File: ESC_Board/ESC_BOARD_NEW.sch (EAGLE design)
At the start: 165 parts, among them J3 AVR_SPI_PROG_3X2NS, U1 FQB27P06, U2 ATMEGA328P_TQFP, U3 FQB27P06, U4 PCA9685

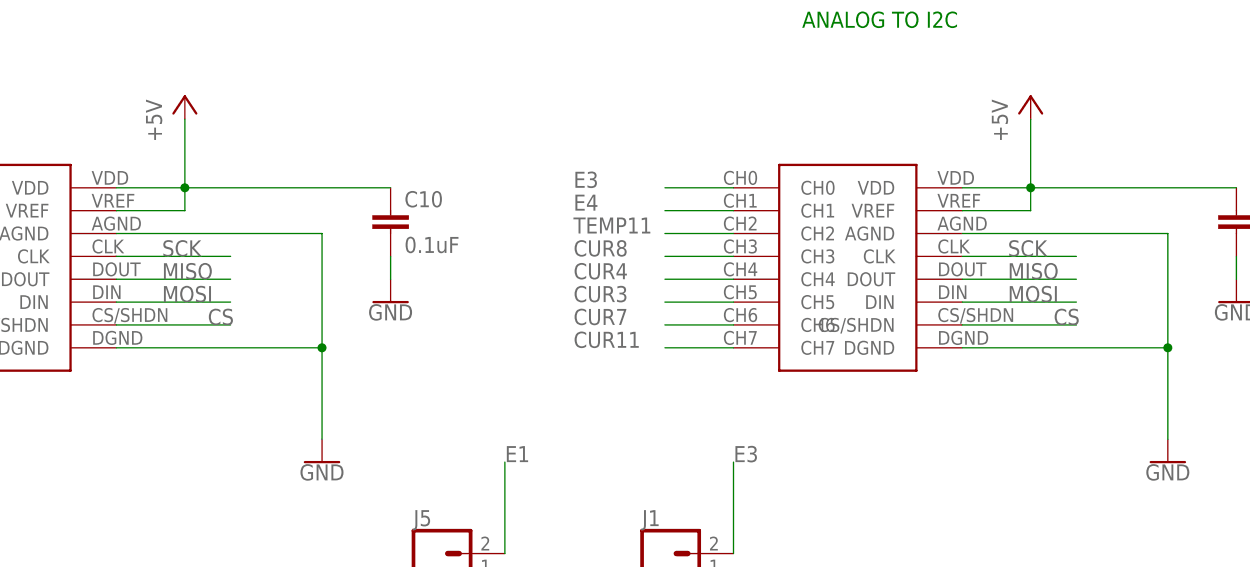
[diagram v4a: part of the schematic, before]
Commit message: Fixing gnd plane and fixing traces
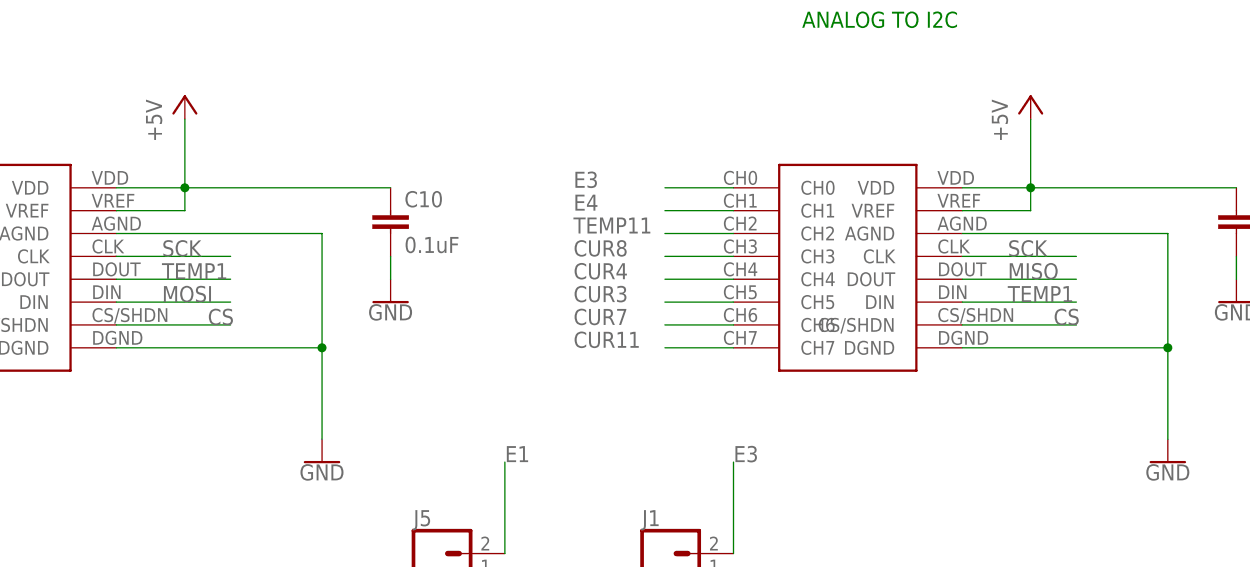
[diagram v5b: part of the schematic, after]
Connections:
- new net TEMP1: U$13.DIN, U$4.DOUT
- net MISO: no longer U$4.DOUT
- net MOSI: no longer U$13.DIN
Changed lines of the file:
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@@
 <?xml version="1.0" encoding="utf-8"?>
 <!DOCTYPE eagle SYSTEM "eagle.dtd">
-<eagle version="8.3.2">
+<eagle version="8.4.3">
 <drawing>
 <settings>
@@
 <label x="-40.64" y="304.8" size="1.778" layer="95"/>
 </segment>
-<segment>
-<pinref part="U$13" gate="G$1" pin="DIN"/>
-<wire x1="48.26" y1="304.8" x2="60.96" y2="304.8" width="0.1524" layer="91"/>
-<label x="53.34" y="304.8" size="1.778" layer="95"/>
-</segment>
 </net>
 <net name="MISO" class="0">
@@
 </segment>
 <segment>
-<pinref part="U$4" gate="G$1" pin="DOUT"/>
-<wire x1="-45.72" y1="307.34" x2="-33.02" y2="307.34" width="0.1524" layer="91"/>
-<label x="-40.64" y="307.34" size="1.778" layer="95"/>
-</segment>
-<segment>
 <pinref part="U$13" gate="G$1" pin="DOUT"/>
 <wire x1="48.26" y1="307.34" x2="60.96" y2="307.34" width="0.1524" layer="91"/>
@@
 </segment>
 </net>
+<net name="TEMP1" class="0">
+<segment>
+<pinref part="U$4" gate="G$1" pin="DOUT"/>
+<wire x1="-45.72" y1="307.34" x2="-33.02" y2="307.34" width="0.1524" layer="91"/>
+<label x="-40.64" y="307.34" size="1.778" layer="95"/>
+</segment>
+<segment>
+<pinref part="U$13" gate="G$1" pin="DIN"/>
+<wire x1="48.26" y1="304.8" x2="60.96" y2="304.8" width="0.1524" layer="91"/>
+<label x="53.34" y="304.8" size="1.778" layer="95"/>
+</segment>
+</net>

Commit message: Adding more test probes and cleaning up crooked traces
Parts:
- added J2, J7: (no value), SparkFun-Connectors:BANANA_CONN
- R10, R26, R27: value (none) -> 10k
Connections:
- net +12V: now also J2.1
- net GND: now also J7.1
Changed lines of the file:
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@@
 <part name="RESET" library="DiscreteComponents" deviceset="SWITCH" device="" value=""/>
 <part name="C11" library="rcl" library_urn="urn:adsk.eagle:library:334" deviceset="C-EU" device="C0603" package3d_urn="urn:adsk.eagle:package:23616/2" value="0.1uF"/>
-<part name="R10" library="SparkFun-Resistors" library_urn="urn:adsk.eagle:library:532" deviceset="RESISTOR" device="0603" package3d_urn="urn:adsk.eagle:package:39650/1" value=" "/>
+<part name="R10" library="SparkFun-Resistors" library_urn="urn:adsk.eagle:library:532" deviceset="RESISTOR" device="0603" package3d_urn="urn:adsk.eagle:package:39650/1" value="10k"/>
 <part name="GND27" library="supply1" deviceset="GND" device=""/>
 <part name="P+13" library="supply1" library_urn="urn:adsk.eagle:library:371" deviceset="+5V" device=""/>
@@
 <part name="C52" library="SparkFun-Capacitors" deviceset="0.1UF" device="-0603-25V-(+80/-20%)" value="0.1uF"/>
 <part name="GND69" library="SparkFun-PowerSymbols" deviceset="GND" device=""/>
-<part name="R26" library="rcl" library_urn="urn:adsk.eagle:library:334" deviceset="R-US_" device="R0603" package3d_urn="urn:adsk.eagle:package:23555/2"/>
-<part name="R27" library="rcl" library_urn="urn:adsk.eagle:library:334" deviceset="R-US_" device="R0603" package3d_urn="urn:adsk.eagle:package:23555/2"/>
+<part name="R26" library="rcl" library_urn="urn:adsk.eagle:library:334" deviceset="R-US_" device="R0603" package3d_urn="urn:adsk.eagle:package:23555/2" value="10k"/>
+<part name="R27" library="rcl" library_urn="urn:adsk.eagle:library:334" deviceset="R-US_" device="R0603" package3d_urn="urn:adsk.eagle:package:23555/2" value="10k"/>
 <part name="P+25" library="supply1" library_urn="urn:adsk.eagle:library:371" deviceset="+5V" device=""/>
 <part name="GND74" library="SparkFun-PowerSymbols" deviceset="GND" device=""/>
@@
 <part name="P14" library="SparkFun-Connectors" deviceset="M01" device="PTH"/>
 <part name="P15" library="SparkFun-Connectors" deviceset="M01" device="PTH"/>
+<part name="P+6" library="supply1" library_urn="urn:adsk.eagle:library:371" deviceset="+5V" device=""/>
+<part name="J2" library="SparkFun-Connectors" deviceset="BANANA_CONN" device=""/>
+<part name="J7" library="SparkFun-Connectors" deviceset="BANANA_CONN" device=""/>
+<part name="P+7" library="supply1" library_urn="urn:adsk.eagle:library:371" deviceset="+12V" device=""/>
+<part name="GND18" library="supply1" deviceset="GND" device=""/>
 </parts>
 <sheets>
@@
 <instance part="P14" gate="G$1" x="86.36" y="375.92" rot="MR0"/>
 <instance part="P15" gate="G$1" x="73.66" y="373.38" rot="MR0"/>
+<instance part="P+6" gate="1" x="-73.66" y="162.56"/>
+<instance part="J2" gate="G$1" x="340.36" y="406.4"/>
+<instance part="J7" gate="G$1" x="340.36" y="401.32"/>
+<instance part="P+7" gate="1" x="325.12" y="411.48"/>
+<instance part="GND18" gate="1" x="325.12" y="396.24"/>
 </instances>
 <busses>
@@
 <wire x1="5.08" y1="50.8" x2="5.08" y2="53.34" width="0.1524" layer="91"/>
 </segment>
+<segment>
+<pinref part="J7" gate="G$1" pin="1"/>
+<wire x1="337.82" y1="401.32" x2="325.12" y2="401.32" width="0.1524" layer="91"/>
+<label x="327.66" y="401.32" size="1.778" layer="95"/>
+<pinref part="GND18" gate="1" pin="GND"/>
+<wire x1="325.12" y1="401.32" x2="325.12" y2="398.78" width="0.1524" layer="91"/>
+</segment>
 </net>
 <net name="+12V" class="0">
@@
 <wire x1="5.08" y1="83.82" x2="5.08" y2="91.44" width="0.1524" layer="91"/>
 <pinref part="P+22" gate="1" pin="+12V"/>
+</segment>
+<segment>
+<pinref part="J2" gate="G$1" pin="1"/>
+<wire x1="337.82" y1="406.4" x2="325.12" y2="406.4" width="0.1524" layer="91"/>
+<label x="327.66" y="406.4" size="1.778" layer="95"/>
+<pinref part="P+7" gate="1" pin="+12V"/>
+<wire x1="325.12" y1="406.4" x2="325.12" y2="408.94" width="0.1524" layer="91"/>
 </segment>
 </net>
@@
 <wire x1="-73.66" y1="157.48" x2="-81.28" y2="157.48" width="0.1524" layer="91"/>
 <junction x="-73.66" y="157.48"/>
-</segment>
-<segment>
+<pinref part="P+6" gate="1" pin="+5V"/>
+</segment>
+<segment>

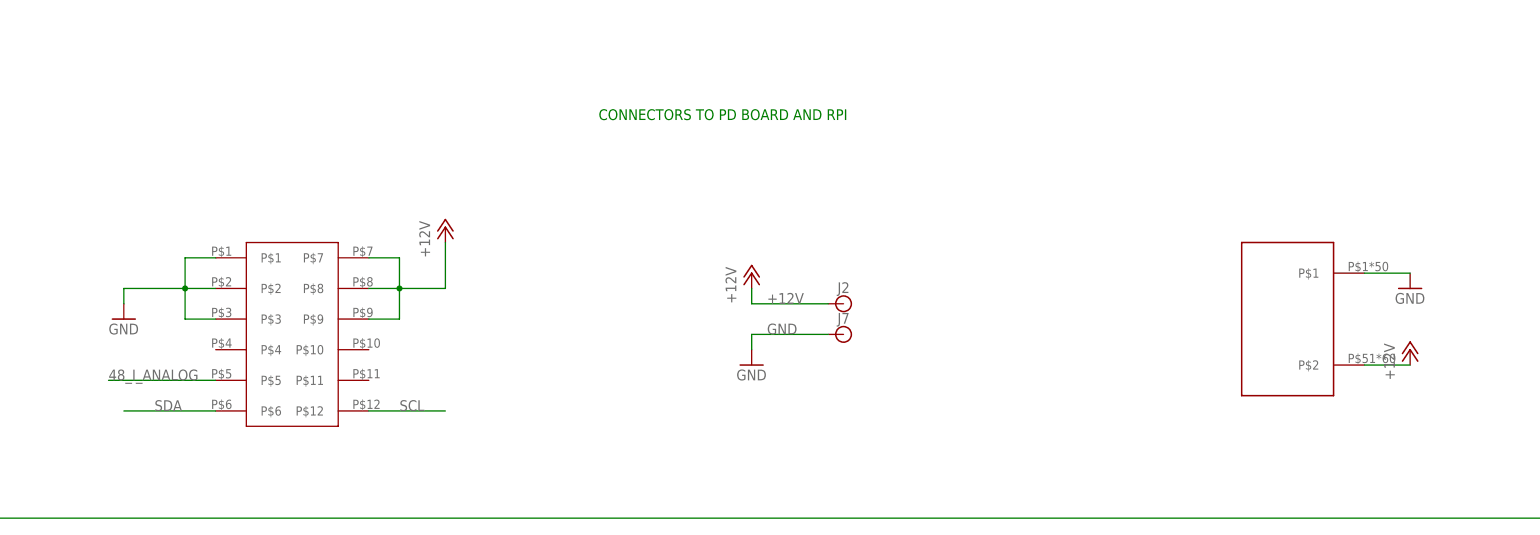
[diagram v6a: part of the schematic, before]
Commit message: Fixed to work with new part
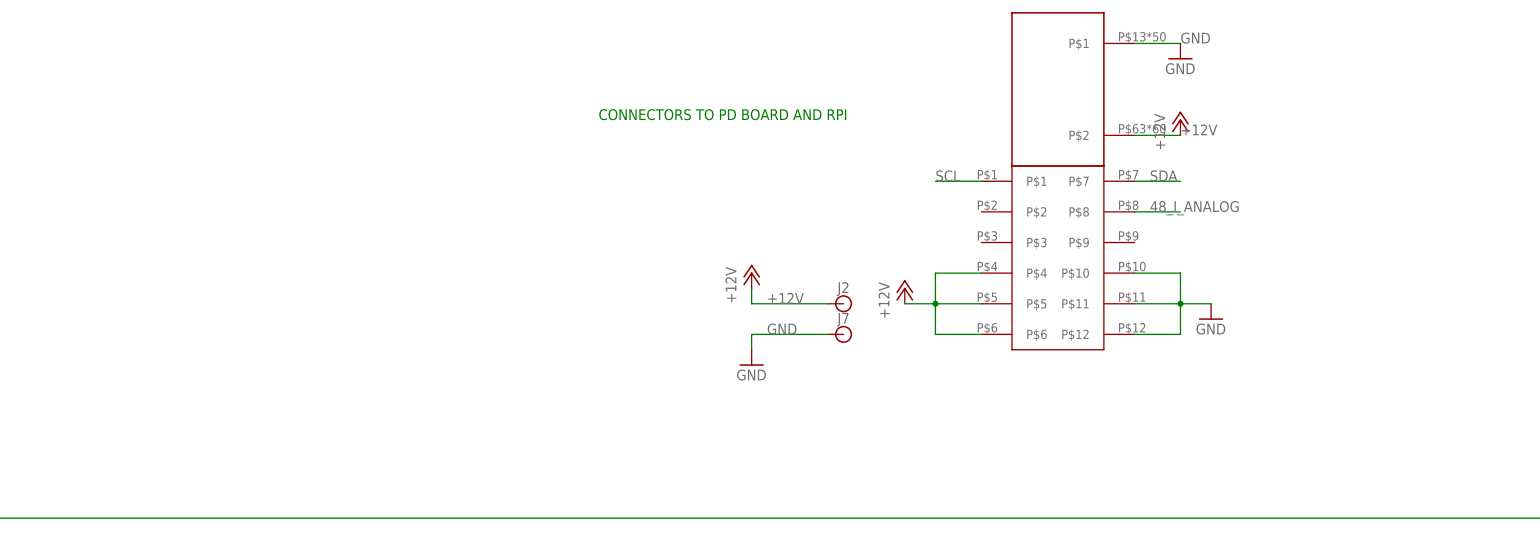
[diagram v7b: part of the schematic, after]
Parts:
- removed U$14: ESC-CONNECTORPARALLELL, MotherboardParts:ESC-CONNECTORPARALLELL
- removed U$16: POWER_BRICK_CONNECTORS(2X6), MotherBoardParts2:POWER_BRICK_CONNECTORS(2X6)
- added U$15: ESC-FULL, MotherboardParts:ESC-FULL
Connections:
- net +12V: now also U$15G$1.P$2, U$15G$2.P$4, U$15G$2.P$5, U$15G$2.P$6; no longer U$14.P$2, U$16.P$7, U$16.P$8, U$16.P$9
- net 48_I_ANALOG: now also U$15G$2.P$8; no longer U$16.P$5
- net GND: now also U$15G$1.P$1, U$15G$2.P$10, U$15G$2.P$11, U$15G$2.P$12; no longer U$14.P$1, U$16.P$1, U$16.P$2, U$16.P$3
- net SCL: now also U$15G$2.P$1; no longer U$16.P$12
- net SDA: now also U$15G$2.P$7; no longer U$16.P$6
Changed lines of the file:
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@@
 <?xml version="1.0" encoding="utf-8"?>
 <!DOCTYPE eagle SYSTEM "eagle.dtd">
-<eagle version="8.4.3">
+<eagle version="8.5.0">
 <drawing>
 <settings>
@@
 <part name="GND94" library="SparkFun-PowerSymbols" deviceset="GND" device=""/>
 <part name="GND95" library="SparkFun-PowerSymbols" deviceset="GND" device=""/>
-<part name="U$16" library="MotherBoardParts2" deviceset="POWER_BRICK_CONNECTORS(2X6)" device=""/>
-<part name="GND" library="supply1" deviceset="GND" device=""/>
 <part name="FRAME5" library="frames" library_urn="urn:adsk.eagle:library:229" deviceset="FRAME_A_L" device=""/>
-<part name="P+32" library="supply1" library_urn="urn:adsk.eagle:library:371" deviceset="+12V" device=""/>
-<part name="P+34" library="supply1" library_urn="urn:adsk.eagle:library:371" deviceset="+12V" device=""/>
-<part name="GND96" library="supply1" deviceset="GND" device=""/>
 <part name="P1" library="SparkFun-Connectors" deviceset="M01" device="PTH"/>
 <part name="P2" library="SparkFun-Connectors" deviceset="M01" device="PTH"/>
@@
 <part name="J1" library="SparkFun-Connectors" deviceset="CONN_02" device=""/>
 <part name="GND19" library="SparkFun-PowerSymbols" deviceset="GND" device=""/>
-<part name="U$14" library="MotherboardParts" deviceset="ESC-CONNECTOR" device="PARALLELL" value="ESC-CONNECTORPARALLELL"/>
 <part name="U1" library="CamSensComponents" deviceset="FQB27P06" device=""/>
 <part name="R5" library="resistor" deviceset="R-US_" device="R0603" value="330"/>
@@
 <part name="P+7" library="supply1" library_urn="urn:adsk.eagle:library:371" deviceset="+12V" device=""/>
 <part name="GND18" library="supply1" deviceset="GND" device=""/>
+<part name="GND21" library="supply1" deviceset="GND" device=""/>
+<part name="GND22" library="supply1" deviceset="GND" device=""/>
+<part name="P+23" library="supply1" deviceset="+12V" device=""/>
+<part name="P+24" library="supply1" deviceset="+12V" device=""/>
+<part name="U$15" library="MotherboardParts" deviceset="ESC-FULL" device=""/>
 </parts>
 <sheets>
@@
 <instance part="GND94" gate="1" x="-157.48" y="106.68"/>
 <instance part="GND95" gate="1" x="-144.78" y="106.68"/>
-<instance part="U$16" gate="G$1" x="248.92" y="406.4"/>
-<instance part="GND" gate="1" x="220.98" y="403.86"/>
 <instance part="FRAME5" gate="G$1" x="185.42" y="246.38"/>
-<instance part="P+32" gate="1" x="274.32" y="419.1"/>
-<instance part="P+34" gate="1" x="434.34" y="398.78"/>
-<instance part="GND96" gate="1" x="434.34" y="408.94"/>
 <instance part="P1" gate="G$1" x="99.06" y="408.94" rot="MR0"/>
 <instance part="P2" gate="G$1" x="86.36" y="406.4" rot="MR0"/>
@@
 <instance part="J1" gate="G$1" x="15.24" y="274.32"/>
 <instance part="GND19" gate="1" x="22.86" y="261.62"/>
-<instance part="U$14" gate="G$1" x="414.02" y="403.86"/>
 <instance part="U1" gate="G$1" x="-71.12" y="78.74"/>
 <instance part="R5" gate="G$1" x="-50.8" y="55.88" rot="R90"/>
@@
 <instance part="P+7" gate="1" x="325.12" y="411.48"/>
 <instance part="GND18" gate="1" x="325.12" y="396.24"/>
+<instance part="GND21" gate="1" x="396.24" y="447.04"/>
+<instance part="GND22" gate="1" x="401.32" y="403.86"/>
+<instance part="P+23" gate="1" x="350.52" y="408.94"/>
+<instance part="P+24" gate="1" x="396.24" y="436.88"/>
+<instance part="U$15" gate="G$1" x="375.92" y="441.96"/>
+<instance part="U$15" gate="G$2" x="373.38" y="408.94"/>
 </instances>
 <busses>
@@
 </segment>
 <segment>
-<pinref part="GND" gate="1" pin="GND"/>
-<wire x1="220.98" y1="406.4" x2="220.98" y2="408.94" width="0.1524" layer="91"/>
-<pinref part="U$16" gate="G$1" pin="P$1"/>
-<wire x1="236.22" y1="414.02" x2="231.14" y2="414.02" width="0.1524" layer="91"/>
-<pinref part="U$16" gate="G$1" pin="P$2"/>
-<wire x1="231.14" y1="414.02" x2="231.14" y2="408.94" width="0.1524" layer="91"/>
-<wire x1="231.14" y1="408.94" x2="236.22" y2="408.94" width="0.1524" layer="91"/>
-<pinref part="U$16" gate="G$1" pin="P$3"/>
-<wire x1="236.22" y1="403.86" x2="231.14" y2="403.86" width="0.1524" layer="91"/>
-<wire x1="231.14" y1="403.86" x2="231.14" y2="408.94" width="0.1524" layer="91"/>
-<junction x="231.14" y="408.94"/>
-<wire x1="220.98" y1="408.94" x2="231.14" y2="408.94" width="0.1524" layer="91"/>
-</segment>
-<segment>
-<pinref part="U$14" gate="G$1" pin="P$1"/>
-<wire x1="426.72" y1="411.48" x2="434.34" y2="411.48" width="0.1524" layer="91"/>
-<pinref part="GND96" gate="1" pin="GND"/>
-</segment>
-<segment>
 <pinref part="LED9" gate="G$1" pin="C"/>
 <pinref part="GND73" gate="1" pin="GND"/>
@@
 <pinref part="GND18" gate="1" pin="GND"/>
 <wire x1="325.12" y1="401.32" x2="325.12" y2="398.78" width="0.1524" layer="91"/>
+</segment>
+<segment>
+<pinref part="U$15" gate="G$1" pin="P$1"/>
+<wire x1="388.62" y1="449.58" x2="396.24" y2="449.58" width="0.1524" layer="91"/>
+<label x="396.24" y="449.58" size="1.778" layer="95"/>
+<pinref part="GND21" gate="1" pin="GND"/>
+</segment>
+<segment>
+<pinref part="U$15" gate="G$2" pin="P$12"/>
+<wire x1="388.62" y1="401.32" x2="396.24" y2="401.32" width="0.1524" layer="91"/>
+<pinref part="U$15" gate="G$2" pin="P$11"/>
+<wire x1="388.62" y1="406.4" x2="396.24" y2="406.4" width="0.1524" layer="91"/>
+<wire x1="396.24" y1="406.4" x2="396.24" y2="401.32" width="0.1524" layer="91"/>
+<pinref part="U$15" gate="G$2" pin="P$10"/>
+<wire x1="388.62" y1="411.48" x2="396.24" y2="411.48" width="0.1524" layer="91"/>
+<wire x1="396.24" y1="411.48" x2="396.24" y2="406.4" width="0.1524" layer="91"/>
+<junction x="396.24" y="406.4"/>
+<wire x1="396.24" y1="406.4" x2="401.32" y2="406.4" width="0.1524" layer="91"/>
+<pinref part="GND22" gate="1" pin="GND"/>
 </segment>
 </net>
@@
 </segment>
 <segment>
-<pinref part="U$16" gate="G$1" pin="P$7"/>
-<wire x1="261.62" y1="414.02" x2="266.7" y2="414.02" width="0.1524" layer="91"/>
-<wire x1="266.7" y1="414.02" x2="266.7" y2="408.94" width="0.1524" layer="91"/>
-<pinref part="U$16" gate="G$1" pin="P$8"/>
-<wire x1="266.7" y1="408.94" x2="261.62" y2="408.94" width="0.1524" layer="91"/>
-<pinref part="U$16" gate="G$1" pin="P$9"/>
-<wire x1="261.62" y1="403.86" x2="266.7" y2="403.86" width="0.1524" layer="91"/>
-<wire x1="266.7" y1="403.86" x2="266.7" y2="408.94" width="0.1524" layer="91"/>
-<junction x="266.7" y="408.94"/>
-<wire x1="266.7" y1="408.94" x2="274.32" y2="408.94" width="0.1524" layer="91"/>
-<pinref part="P+32" gate="1" pin="+12V"/>
-<wire x1="274.32" y1="408.94" x2="274.32" y2="416.56" width="0.1524" layer="91"/>
-</segment>
-<segment>
-<pinref part="U$14" gate="G$1" pin="P$2"/>
-<wire x1="426.72" y1="396.24" x2="434.34" y2="396.24" width="0.1524" layer="91"/>
-<pinref part="P+34" gate="1" pin="+12V"/>
-</segment>
-<segment>
 <pinref part="U1" gate="G$1" pin="S2"/>
 <wire x1="-58.42" y1="83.82" x2="-58.42" y2="91.44" width="0.1524" layer="91"/>
@@
 <pinref part="P+7" gate="1" pin="+12V"/>
 <wire x1="325.12" y1="406.4" x2="325.12" y2="408.94" width="0.1524" layer="91"/>
+</segment>
+<segment>
+<pinref part="U$15" gate="G$1" pin="P$2"/>
+<wire x1="388.62" y1="434.34" x2="396.24" y2="434.34" width="0.1524" layer="91"/>
+<label x="396.24" y="434.34" size="1.778" layer="95"/>
+<pinref part="P+24" gate="1" pin="+12V"/>
+</segment>
+<segment>
+<pinref part="U$15" gate="G$2" pin="P$4"/>
+<wire x1="363.22" y1="411.48" x2="355.6" y2="411.48" width="0.1524" layer="91"/>
+<wire x1="355.6" y1="411.48" x2="355.6" y2="406.4" width="0.1524" layer="91"/>
+<pinref part="U$15" gate="G$2" pin="P$6"/>
+<wire x1="355.6" y1="406.4" x2="355.6" y2="401.32" width="0.1524" layer="91"/>
+<wire x1="355.6" y1="401.32" x2="363.22" y2="401.32" width="0.1524" layer="91"/>
+<pinref part="U$15" gate="G$2" pin="P$5"/>
+<wire x1="363.22" y1="406.4" x2="355.6" y2="406.4" width="0.1524" layer="91"/>
+<junction x="355.6" y="406.4"/>
+<wire x1="355.6" y1="406.4" x2="350.52" y2="406.4" width="0.1524" layer="91"/>
+<pinref part="P+23" gate="1" pin="+12V"/>
 </segment>
 </net>
@@
 </segment>
 <segment>
-<pinref part="U$16" gate="G$1" pin="P$6"/>
-<wire x1="236.22" y1="388.62" x2="220.98" y2="388.62" width="0.1524" layer="91"/>
-<label x="226.06" y="388.62" size="1.778" layer="95"/>
+<pinref part="U$15" gate="G$2" pin="P$7"/>
+<wire x1="388.62" y1="426.72" x2="396.24" y2="426.72" width="0.1524" layer="91"/>
+<label x="391.16" y="426.72" size="1.778" layer="95"/>
 </segment>
 </net>
@@
 </segment>
 <segment>
-<pinref part="U$16" gate="G$1" pin="P$12"/>
-<wire x1="261.62" y1="388.62" x2="274.32" y2="388.62" width="0.1524" layer="91"/>
-<label x="266.7" y="388.62" size="1.778" layer="95"/>
+<pinref part="U$15" gate="G$2" pin="P$1"/>
+<wire x1="363.22" y1="426.72" x2="355.6" y2="426.72" width="0.1524" layer="91"/>
+<label x="355.6" y="426.72" size="1.778" layer="95"/>
 </segment>
 </net>
@@
 <net name="48_I_ANALOG" class="0">
 <segment>
-<pinref part="U$16" gate="G$1" pin="P$5"/>
-<wire x1="236.22" y1="393.7" x2="218.44" y2="393.7" width="0.1524" layer="91"/>
-<label x="218.44" y="393.7" size="1.778" layer="95"/>
-</segment>
-<segment>
 <pinref part="U$4" gate="G$1" pin="CH7"/>
 <wire x1="-71.12" y1="299.72" x2="-78.74" y2="299.72" width="0.1524" layer="91"/>
 <label x="-91.44" y="299.72" size="1.778" layer="95"/>
 </segment>
-</net>
+<segment>
+<pinref part="U$15" gate="G$2" pin="P$8"/>
+<wire x1="388.62" y1="421.64" x2="396.24" y2="421.64" width="0.1524" layer="91"/>
+<label x="391.16" y="421.64" size="1.778" layer="95"/>
+</segment>
+</net>
